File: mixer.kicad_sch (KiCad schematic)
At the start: 40 parts, among them T1 RF_BALUN, T2 RF_BALUN, U4 RFFC5072, U5 FM8625H, U6 FM8625H

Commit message: Improve power supply filtering and decoupling
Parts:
- C1, C25, C28, C3, C41, C42, C46, C49, C5, C7, C8: value 1uF -> 1 uF
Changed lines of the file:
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@@
 			)
 		)
-		(property "Value" "1uF"
+		(property "Value" "1 uF"
 			(at 135.89 185.4199 0)
 			(effects
@@
 			)
 		)
-		(property "Value" "1uF"
+		(property "Value" "1 uF"
 			(at 213.36 88.9 90)
 			(effects
@@
 			)
 		)
-		(property "Value" "1uF"
+		(property "Value" "1 uF"
 			(at 113.03 185.4199 0)
 			(effects
@@
 			)
 		)
-		(property "Value" "1uF"
+		(property "Value" "1 uF"
 			(at 44.45 185.4199 0)
 			(effects
@@
 			)
 		)
-		(property "Value" "1uF"
+		(property "Value" "1 uF"
 			(at 81.28 92.71 90)
 			(effects
@@
 			)
 		)
-		(property "Value" "1uF"
+		(property "Value" "1 uF"
 			(at 213.36 104.1399 0)
 			(effects
@@
 			)
 		)
-		(property "Value" "1uF"
+		(property "Value" "1 uF"
 			(at 80.01 77.4699 0)
 			(effects
@@
 			)
 		)
-		(property "Value" "1uF"
+		(property "Value" "1 uF"
 			(at 55.88 185.4199 0)
 			(effects
@@
 			)
 		)
-		(property "Value" "1uF"
+		(property "Value" "1 uF"
 			(at 124.46 185.4199 0)
 			(effects
@@
 			)
 		)
-		(property "Value" "1uF"
+		(property "Value" "1 uF"
 			(at 99.06 186.69 0)
 			(effects
@@
 			)
 		)
-		(property "Value" "1uF"
+		(property "Value" "1 uF"
 			(at 147.32 185.4199 0)
 			(effects

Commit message: Update component selections
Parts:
- C12, C13: Manufacturer Murata -> Murata
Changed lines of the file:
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@@
 			)
 		)
-		(property "Manufacturer" "Murata "
+		(property "Manufacturer" "Murata"
 			(at 158.75 43.18 0)
 			(effects
@@
 			)
 		)
-		(property "Manufacturer" "Murata "
+		(property "Manufacturer" "Murata"
 			(at 163.83 43.18 0)
 			(effects

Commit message: Change L1 from 0201 to 0603
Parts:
- L1: footprint Inductor_SMD:L_0201_0603Metric -> Inductor_SMD:L_0603_1608Metric
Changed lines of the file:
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@@
 			)
 		)
-		(property "Footprint" "Inductor_SMD:L_0201_0603Metric"
+		(property "Footprint" "Inductor_SMD:L_0603_1608Metric"
 			(at 114.3 80.01 0)
 			(effects

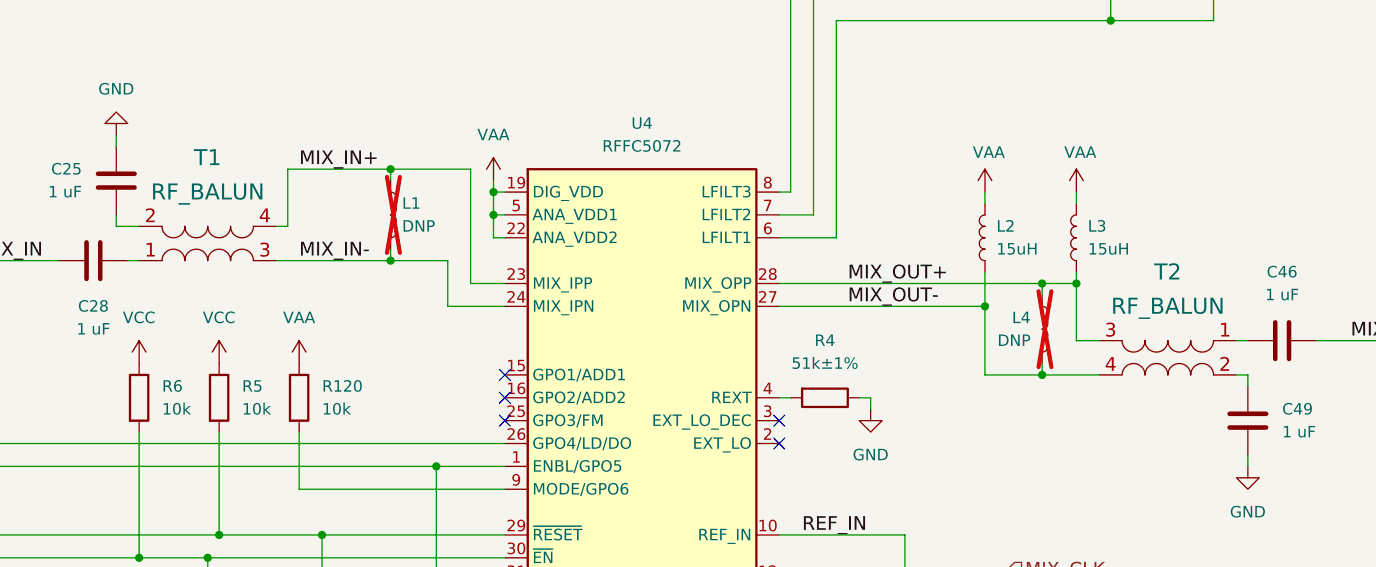
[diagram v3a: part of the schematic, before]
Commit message: Update to KiCad 9
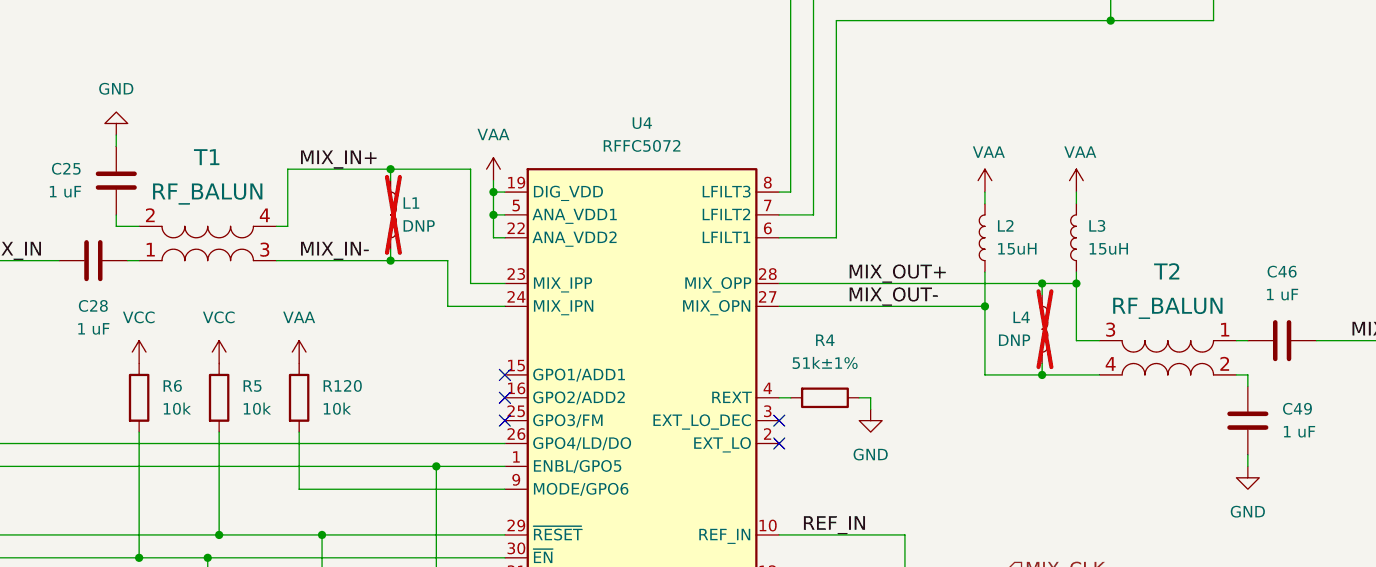
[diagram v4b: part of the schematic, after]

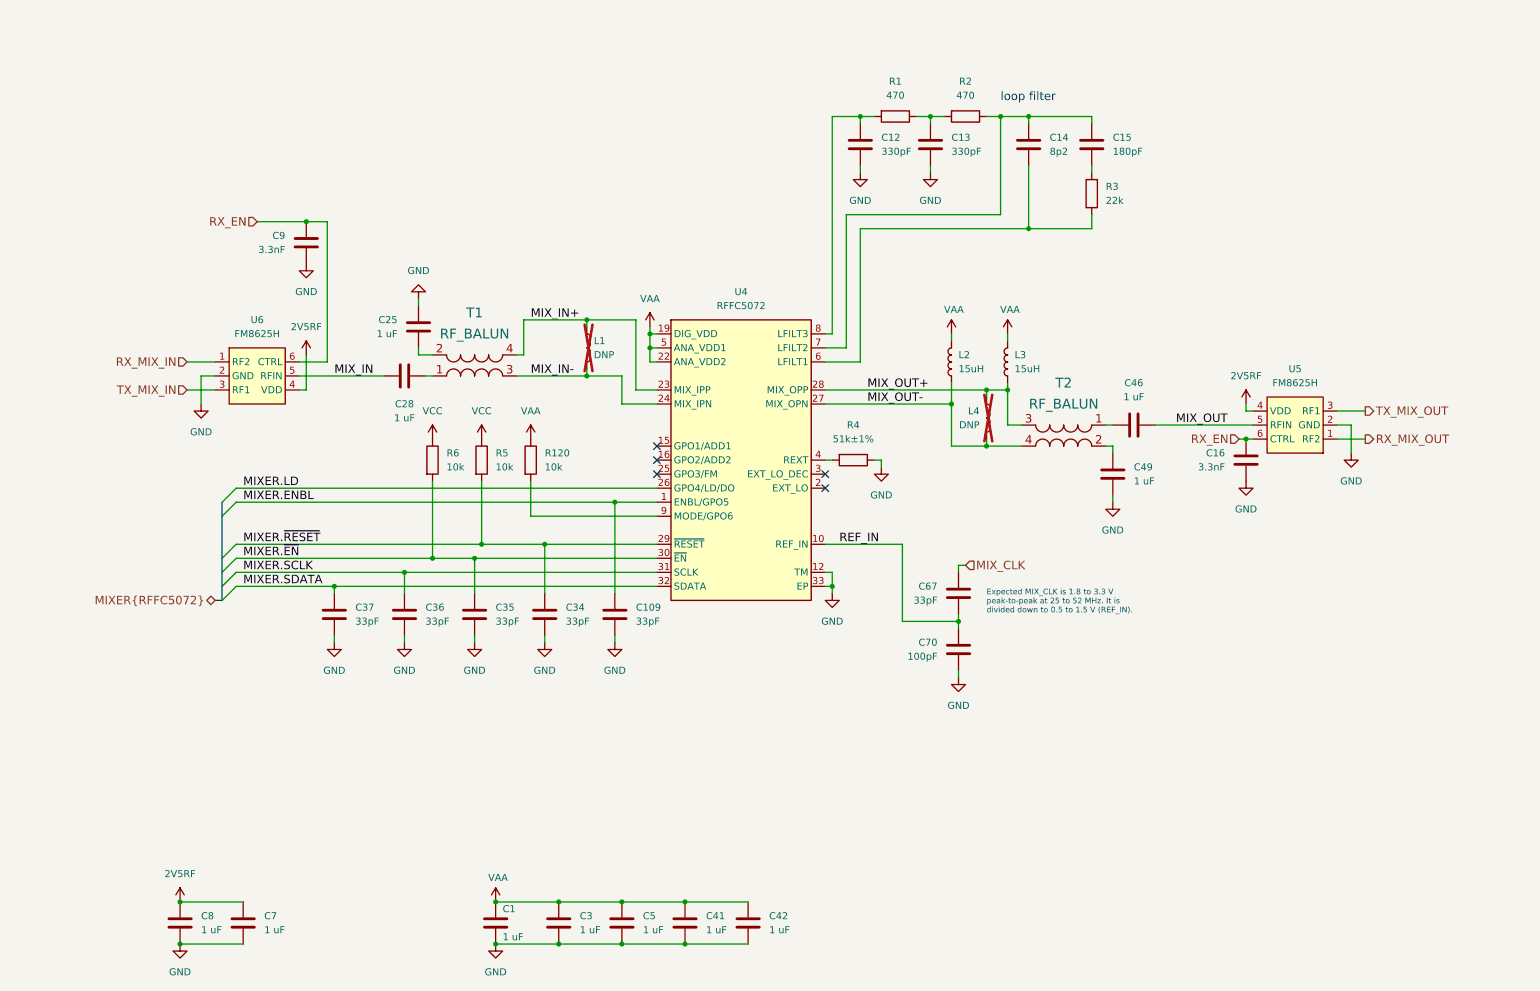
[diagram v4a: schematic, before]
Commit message: Widen mixer output bias tee frequency range
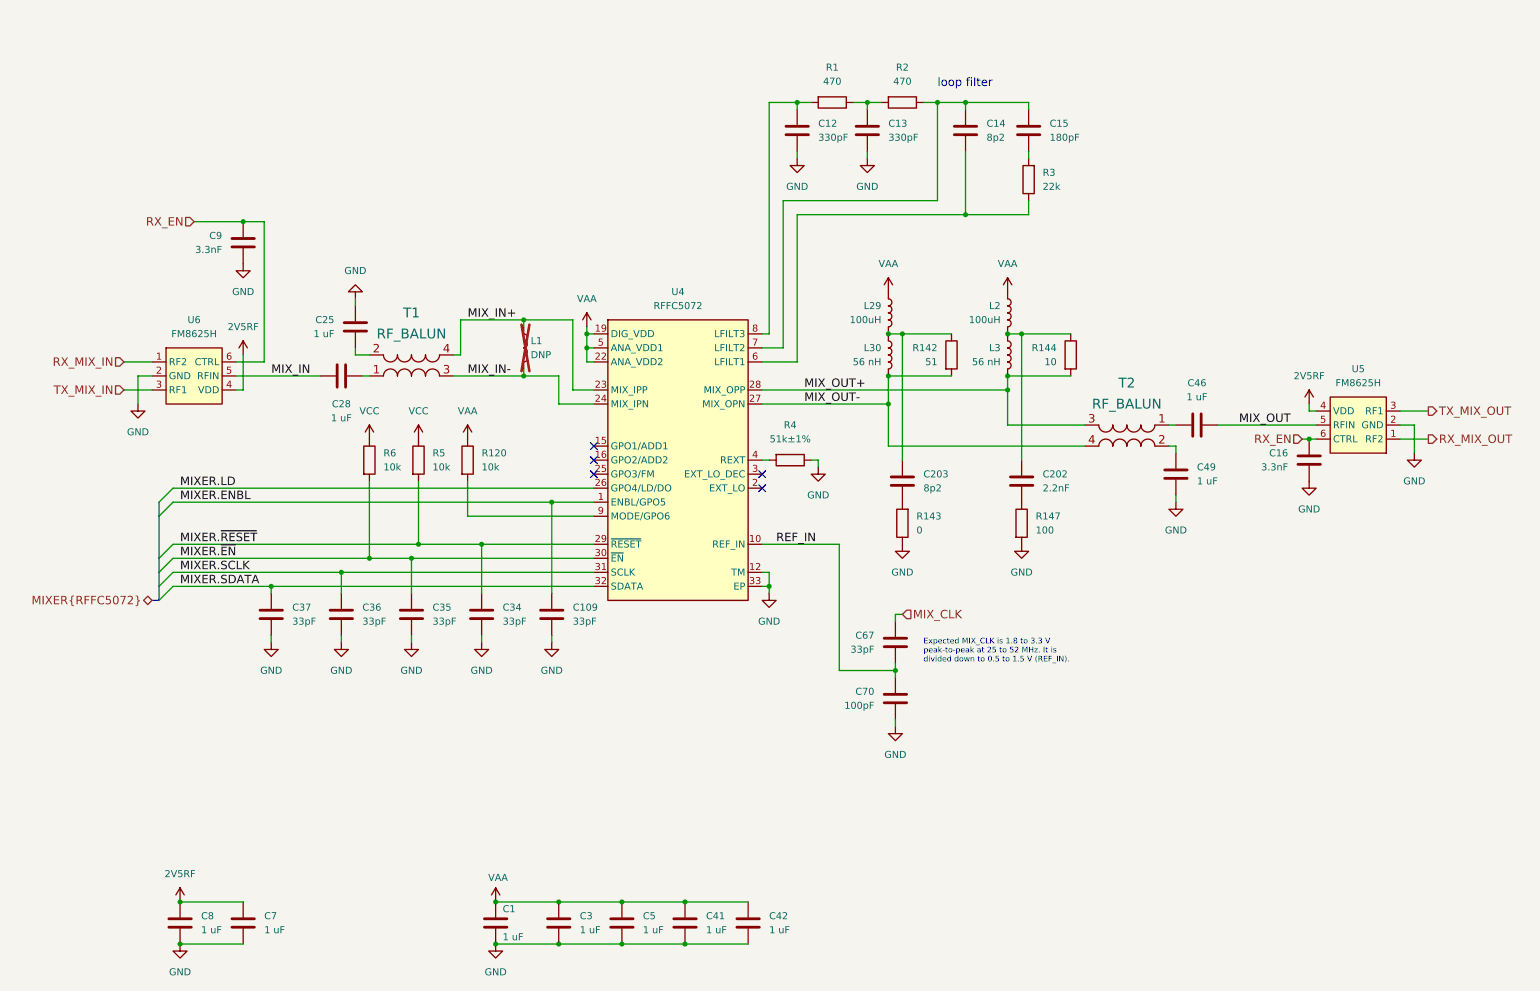
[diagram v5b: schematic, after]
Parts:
- removed L4: DNP, Inductor_SMD:L_0201_0603Metric, symbol Device:L
- added C202: 2.2nF, Capacitor_SMD:C_0201_0603Metric, symbol Device:C
- added C203: 8p2, Capacitor_SMD:C_0201_0603Metric, symbol Device:C
- added L29: 100uH, praline:L_TDK_MLZ2012_h1.25mm, symbol Device:L
- added L30: 56 nH, Inductor_SMD:L_0201_0603Metric, symbol Device:L
- added R142: 51, Resistor_SMD:R_0201_0603Metric, symbol Device:R
- added R143: 0, Resistor_SMD:R_0201_0603Metric, symbol Device:R
- added R144: 10, Resistor_SMD:R_0201_0603Metric, symbol Device:R
- added R147: 100, Resistor_SMD:R_0201_0603Metric, symbol Device:R
- L2: value 15uH -> 100uH; footprint Inductor_SMD:L_0603_1608Metric -> praline:L_TDK_MLZ2012_h1.25mm; Manufacturer Taiyo Yuden -> TDK; Part Number LSQPB160807T150M -> MLZ2012N101LT000; Substitution BRL1608T150M, LLQPB160807T150M -> MLZ2012N101LTD25
- L3: value 15uH -> 56 nH; footprint Inductor_SMD:L_0603_1608Metric -> Inductor_SMD:L_0201_0603Metric; Manufacturer Taiyo Yuden -> Murata; Part Number LSQPB160807T150M -> LQP03TN56NJ02D; Substitution BRL1608T150M, LLQPB160807T150M -> LQP03TN56NH02D
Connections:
- net GND: now also R143.1, R147.2
- net MIX_OUT+: now also L3.2, R144.2; no longer L3.1
- net MIX_OUT-: now also L30.2, R142.2; no longer L2.1
- net VAA: now also L2.1, L29.1; no longer L2.2, L3.2
- new net: C203.1, L29.2, L30.1, R142.1
- new net: C203.2, R143.2
- new net: C202.2, L2.2, L3.1, R144.1
- new net: C202.1, R147.1
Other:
- moved on the sheet: C109, C12, C13, C14, C15, C16, C25, C28, C34, C35, C36, C37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

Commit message: Update symbols and footprints
- Update U21 symbol and footprint
- Add L10, L11 3D model
- Add T1, T2 3D model
- Update U29 footprint
- Update J10 footprint and part selection, change to TP6
- Update diode footprints and 3D models
- Update SMA connector footprint
- Fix 3D model scale for various footprints
- Change L1 from 0603 back to 0201
- Fix pin header 3D models
- Add component substitutions
- Update RF switch and amplifier footprints
- Remove fiducials
- Update mounting hole symbol and footprint
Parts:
- L1: footprint Inductor_SMD:L_0603_1608Metric -> Inductor_SMD:L_0201_0603Metric
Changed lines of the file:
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@@
 			)
 		)
-		(property "Footprint" "Inductor_SMD:L_0603_1608Metric"
+		(property "Footprint" "Inductor_SMD:L_0201_0603Metric"
 			(at 102.87 80.01 0)
 			(effects

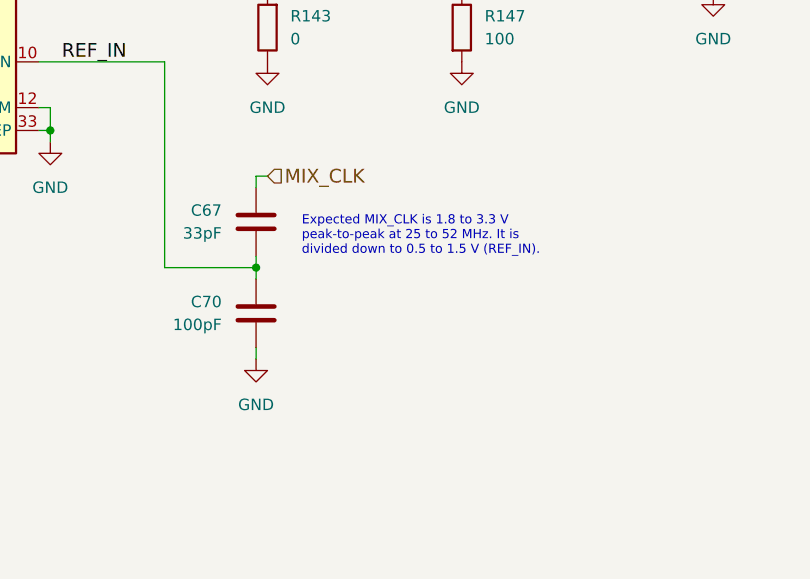
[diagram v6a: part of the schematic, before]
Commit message: Add XCVR_CLK and MIX_CLK passive options
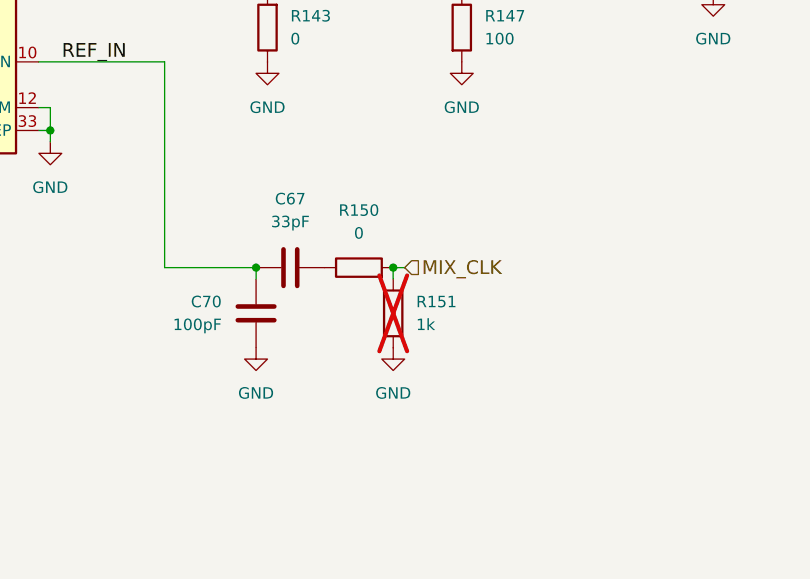
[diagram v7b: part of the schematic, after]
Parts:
- added R150: 0, Resistor_SMD:R_0201_0603Metric, symbol Device:R
- added R151: 1k, Resistor_SMD:R_0201_0603Metric, symbol Device:R
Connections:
- net GND: now also R151.2
- net MIX_CLK: now also R150.2, R151.1; no longer C67.1
- new net: C67.1, R150.1
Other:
- note removed: "Expected MIX_CLK is 1.8 to 3.3 V peak-to-peak at 25 to 52 MHz. It is divided down to 0.5 to 1.5 V (REF_IN)."
- moved on the sheet: C67
